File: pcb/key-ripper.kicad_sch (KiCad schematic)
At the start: 197 parts, among them J1 Conn_01x03, SW1 ESC, SW10 F9, SW11 F10, SW12 F11, SW13 F12, SW14 TILDE, SW15 1, SW16 2, SW17 3, SW18 4, SW19 5, SW2 F1, SW20 6, SW21 7, SW22 8, SW23 9, SW24 0, SW25 -, SW26 =, SW27 BACKSPACE, SW28 TAB, SW29 Q, SW3 F2, SW30 W, SW31 E, SW32 R, SW33 T, SW34 Y, SW35 U, SW36 I, SW37 O, SW38 P, SW39 [, SW4 F3, SW40 ], SW41 \, SW42 CAPS, SW43 A, SW44 S, SW45 D, SW46 F, SW47 G, SW48 H, SW49 J, SW5 F4, SW50 K, SW51 L, SW52 ;, SW53 ', SW54 ENTER, SW55 L_SHIFT, SW56 Z, SW57 X, SW58 C, SW59 V, SW6 F5, SW60 B, SW61 N, SW62 M, SW63 ,, SW64 ., SW65 /, SW66 UP, SW67 FN, SW68 BL_CTRL, SW69 L_ALT, SW7 F6, SW70 L_CMD, SW71 SPACE, SW72 R_CMD, SW73 LEFT, SW74 DOWN, SW75 RIGHT, SW8 F7, SW9 F8, U1 RP2040, U2 TYPE-C-31-M-12, U3 XC6206PxxxMR, U4 W25Q128JVS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

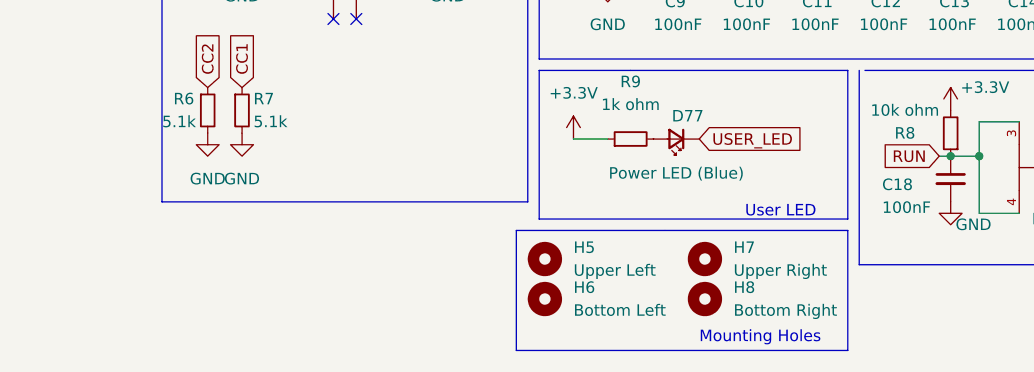
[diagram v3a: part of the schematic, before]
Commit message: Add M2 spacer pass-through mounting holes to the schematic
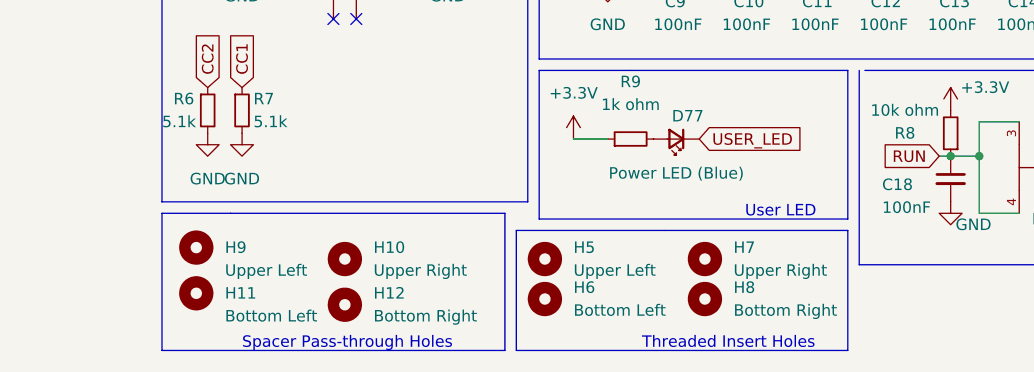
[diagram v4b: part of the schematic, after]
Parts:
- added H10: Upper Right, footprints:m2_hex_spacer_passthrough, symbol Mechanical:MountingHole
- added H11: Bottom Left, footprints:m2_hex_spacer_passthrough, symbol Mechanical:MountingHole
- added H12: Bottom Right, footprints:m2_hex_spacer_passthrough, symbol Mechanical:MountingHole
- added H9: Upper Left, footprints:m2_hex_spacer_passthrough, symbol Mechanical:MountingHole
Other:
- note added: "Spacer Pass-through Holes"
- note added: "Threaded Insert Holes"
- note removed: "Mounting Holes"
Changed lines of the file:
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@@
     (stroke (width 0) (type default) (color 0 0 0 0))
   )
+  (polyline (pts (xy 50.8 195.58) (xy 12.7 195.58))
+    (stroke (width 0) (type default) (color 0 0 0 0))
+  )
   (wire (pts (xy 22.86 92.71) (xy 26.67 92.71))
     (stroke (width 0) (type default) (color 0 0 0 0))
@@
     (stroke (width 0) (type default) (color 0 0 0 0))
   )
+  (polyline (pts (xy 50.8 180.34) (xy 50.8 195.58))
+    (stroke (width 0) (type default) (color 0 0 0 0))
+  )
   (wire (pts (xy 143.51 36.83) (xy 143.51 49.53))
     (stroke (width 0) (type default) (color 0 0 0 0))
@@
     (stroke (width 0) (type default) (color 0 0 0 0))
   )
+  (polyline (pts (xy 20.32 180.34) (xy 50.8 180.34))
+    (stroke (width 0) (type default) (color 0 0 0 0))
+  )
   (wire (pts (xy 113.03 62.23) (xy 113.03 74.93))
     (stroke (width 0) (type default) (color 0 0 0 0))
@@
     (stroke (width 0) (type default) (color 0 0 0 0))
   )
+  (polyline (pts (xy 12.7 180.34) (xy 20.32 180.34))
+    (stroke (width 0) (type default) (color 0 0 0 0))
+  )
   (wire (pts (xy -1.905 55.88) (xy 0.635 55.88))
     (stroke (width 0) (type default) (color 0 0 0 0))
@@
     (stroke (width 0) (type default) (color 0 0 0 0))
   )
+  (polyline (pts (xy 12.7 195.58) (xy 12.7 180.34))
+    (stroke (width 0) (type default) (color 0 0 0 0))
+  )
   (wire (pts (xy 231.775 123.19) (xy 231.775 118.745))
     (stroke (width 0) (type default) (color 0 0 0 0))
@@
     (effects (font (size 1.27 1.27)) (justify left bottom))
   )
-  (text "Mounting Holes" (at 72.39 194.945 0)
+  (text "Threaded Insert Holes" (at 66.04 195.58 0)
     (effects (font (size 1.27 1.27)) (justify left bottom))
   )
@@
     (effects (font (size 1.27 1.27)) (justify left bottom))
   )
+  (text "Spacer Pass-through Holes" (at 21.59 195.58 0)
+    (effects (font (size 1.27 1.27)) (justify left bottom))
+  )
   (text "Serial Wire Debug" (at 171.45 139.065 0)
     (effects (font (size 1.27 1.27)) (justify left bottom))
@@
     (pin "2")
   )
+  (symbol (lib_id "Mechanical:MountingHole") (at 33.02 185.42 0) (unit 1)
+    (in_bom yes) (on_board yes) (fields_autoplaced)
+    (property "Reference" "H10" (id 0) (at 36.195 184.1499 0)
+      (effects (font (size 1.27 1.27)) (justify left))
+    )
+    (property "Value" "Upper Right" (id 1) (at 36.195 186.6899 0)
+      (effects (font (size 1.27 1.27)) (justify left))
+    )
+    (property "Footprint" "footprints:m2_hex_spacer_passthrough" (id 2) (at 33.02 185.42 0)
+      (effects (font (size 1.27 1.27)) hide)
+    )
+    (property "Datasheet" "~" (id 3) (at 33.02 185.42 0)
+      (effects (font (size 1.27 1.27)) hide)
+    )
+  )
   (symbol (lib_id "Device:C_Small") (at 120.015 125.73 0) (unit 1)
     (in_bom yes) (on_board yes) (fields_autoplaced)
@@
     (pin "1")
   )
+  (symbol (lib_id "Mechanical:MountingHole") (at 33.02 190.5 0) (unit 1)
+    (in_bom yes) (on_board yes) (fields_autoplaced)
+    (property "Reference" "H12" (id 0) (at 36.195 189.2299 0)
+      (effects (font (size 1.27 1.27)) (justify left))
+    )
+    (property "Value" "Bottom Right" (id 1) (at 36.195 191.7699 0)
+      (effects (font (size 1.27 1.27)) (justify left))
+    )
+    (property "Footprint" "footprints:m2_hex_spacer_passthrough" (id 2) (at 33.02 190.5 0)
+      (effects (font (size 1.27 1.27)) hide)
+    )
+    (property "Datasheet" "~" (id 3) (at 33.02 190.5 0)
+      (effects (font (size 1.27 1.27)) hide)
+    )
+  )
   (symbol (lib_id "Device:D_Small") (at 72.39 77.47 90) (unit 1)
     (in_bom yes) (on_board yes)
@@
     (pin "2")
   )
+  (symbol (lib_id "Mechanical:MountingHole") (at 16.51 184.15 0) (unit 1)
+    (in_bom yes) (on_board yes)
+    (property "Reference" "H9" (id 0) (at 19.685 184.1499 0)
+      (effects (font (size 1.27 1.27)) (justify left))
+    )
+    (property "Value" "Upper Left" (id 1) (at 19.685 186.6899 0)
+      (effects (font (size 1.27 1.27)) (justify left))
+    )
+    (property "Footprint" "footprints:m2_hex_spacer_passthrough" (id 2) (at 16.51 184.15 0)
+      (effects (font (size 1.27 1.27)) hide)
+    )
+    (property "Datasheet" "~" (id 3) (at 16.51 184.15 0)
+      (effects (font (size 1.27 1.27)) hide)
+    )
+  )
   (symbol (lib_id "Device:C_Small") (at 107.95 151.765 0) (unit 1)
     (in_bom yes) (on_board yes)
@@
     (pin "2")
   )
+  (symbol (lib_id "Mechanical:MountingHole") (at 16.51 189.23 0) (unit 1)
+    (in_bom yes) (on_board yes)
+    (property "Reference" "H11" (id 0) (at 19.685 189.2299 0)
+      (effects (font (size 1.27 1.27)) (justify left))
+    )
+    (property "Value" "Bottom Left" (id 1) (at 19.685 191.7699 0)
+      (effects (font (size 1.27 1.27)) (justify left))
+    )
+    (property "Footprint" "footprints:m2_hex_spacer_passthrough" (id 2) (at 16.51 189.23 0)
+      (effects (font (size 1.27 1.27)) hide)
+    )
+    (property "Datasheet" "~" (id 3) (at 16.51 189.23 0)
+      (effects (font (size 1.27 1.27)) hide)
+    )
+  )
   (symbol (lib_id "Switch:SW_Push") (at 62.23 49.53 0) (unit 1)
     (in_bom yes) (on_board yes) (fields_autoplaced)
@@
       (reference "H8") (unit 1) (value "Bottom Right") (footprint "footprints:threaded_insert_m3_24939")
     )
+    (path "/b908f0d6-f276-4b53-8757-77900b0c31c4"
+      (reference "H9") (unit 1) (value "Upper Left") (footprint "footprints:m2_hex_spacer_passthrough")
+    )
+    (path "/751c73b9-913c-424a-a0fb-30ecc4a69248"
+      (reference "H10") (unit 1) (value "Upper Right") (footprint "footprints:m2_hex_spacer_passthrough")
+    )
+    (path "/c2a76fc2-6b67-49a3-ada5-bc5364302220"
+      (reference "H11") (unit 1) (value "Bottom Left") (footprint "footprints:m2_hex_spacer_passthrough")
+    )
+    (path "/7e1e60e5-bf93-4fda-b4a7-96c7ffe3f045"
+      (reference "H12") (unit 1) (value "Bottom Right") (footprint "footprints:m2_hex_spacer_passthrough")
+    )
     (path "/1b5afd94-2096-4603-93d6-8693d1fb5da2"

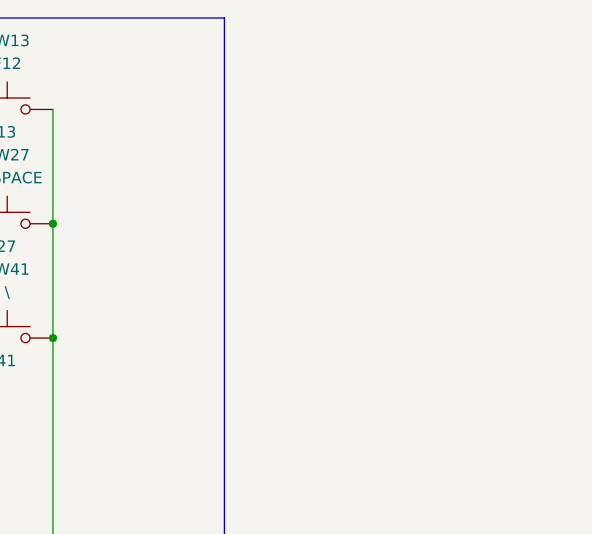
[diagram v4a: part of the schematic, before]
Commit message: Add footprints for the hex spacer pass-through edge cuts
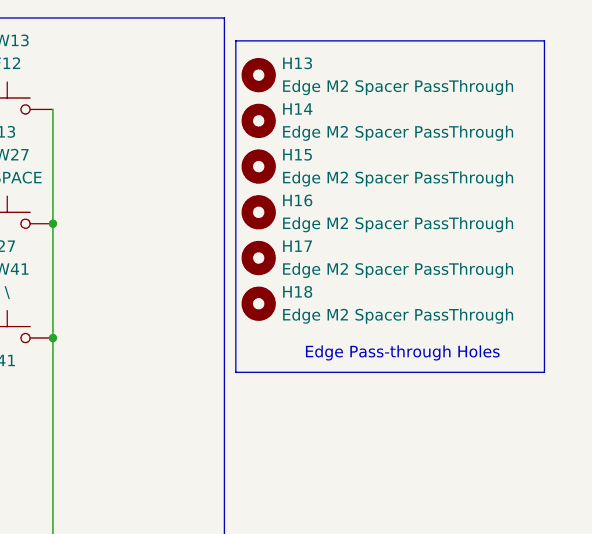
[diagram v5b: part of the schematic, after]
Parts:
- added H13, H14, H15, H16, H17, H18: Edge M2 Spacer PassThrough, footprints:m2_hex_spacer_passthrough_edge, symbol Mechanical:MountingHole
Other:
- note added: "Edge Pass-through Holes"
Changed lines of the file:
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@@
     (stroke (width 0) (type default) (color 0 0 0 0))
   )
+  (polyline (pts (xy 255.27 16.51) (xy 289.56 16.51))
+    (stroke (width 0) (type default) (color 0 0 0 0))
+  )
   (polyline (pts (xy 50.8 180.34) (xy 50.8 195.58))
     (stroke (width 0) (type default) (color 0 0 0 0))
@@
     (stroke (width 0) (type default) (color 0 0 0 0))
   )
+  (polyline (pts (xy 255.27 16.51) (xy 255.27 53.34))
+    (stroke (width 0) (type default) (color 0 0 0 0))
+  )
   (wire (pts (xy 77.47 154.305) (xy 85.09 154.305))
     (stroke (width 0) (type default) (color 0 0 0 0))
@@
     (stroke (width 0) (type default) (color 0 0 0 0))
   )
+  (polyline (pts (xy 289.56 16.51) (xy 289.56 53.34))
+    (stroke (width 0) (type default) (color 0 0 0 0))
+  )
   (wire (pts (xy 102.87 41.91) (xy 118.11 41.91))
     (stroke (width 0) (type default) (color 0 0 0 0))
@@
     (stroke (width 0) (type default) (color 0 0 0 0))
   )
+  (polyline (pts (xy 289.56 53.34) (xy 255.27 53.34))
+    (stroke (width 0) (type default) (color 0 0 0 0))
+  )
   (wire (pts (xy -38.1 43.18) (xy -41.91 43.18))
     (stroke (width 0) (type default) (color 0 0 0 0))
@@
     (effects (font (size 1.27 1.27)) (justify left bottom))
   )
+  (text "Edge Pass-through Holes" (at 262.89 52.07 0)
+    (effects (font (size 1.27 1.27)) (justify left bottom))
+  )
   (text "Stabilizers" (at 147.32 187.325 0)
     (effects (font (size 1.27 1.27)) (justify left bottom))
@@
     (pin "B9")
   )
+  (symbol (lib_id "Mechanical:MountingHole") (at 257.81 20.32 0) (unit 1)
+    (in_bom yes) (on_board yes) (fields_autoplaced)
+    (property "Reference" "H13" (id 0) (at 260.35 19.0499 0)
+      (effects (font (size 1.27 1.27)) (justify left))
+    )
+    (property "Value" "Edge M2 Spacer PassThrough" (id 1) (at 260.35 21.5899 0)
+      (effects (font (size 1.27 1.27)) (justify left))
+    )
+    (property "Footprint" "footprints:m2_hex_spacer_passthrough_edge" (id 2) (at 257.81 20.32 0)
+      (effects (font (size 1.27 1.27)) hide)
+    )
+    (property "Datasheet" "~" (id 3) (at 257.81 20.32 0)
+      (effects (font (size 1.27 1.27)) hide)
+    )
+  )
   (symbol (lib_id "Device:D_Small") (at 133.35 26.67 90) (unit 1)
     (in_bom yes) (on_board yes)
@@
     (pin "1")
   )
+  (symbol (lib_id "Mechanical:MountingHole") (at 257.81 30.48 0) (unit 1)
+    (in_bom yes) (on_board yes) (fields_autoplaced)
+    (property "Reference" "H15" (id 0) (at 260.35 29.2099 0)
+      (effects (font (size 1.27 1.27)) (justify left))
+    )
+    (property "Value" "Edge M2 Spacer PassThrough" (id 1) (at 260.35 31.7499 0)
+      (effects (font (size 1.27 1.27)) (justify left))
+    )
+    (property "Footprint" "footprints:m2_hex_spacer_passthrough_edge" (id 2) (at 257.81 30.48 0)
+      (effects (font (size 1.27 1.27)) hide)
+    )
+    (property "Datasheet" "~" (id 3) (at 257.81 30.48 0)
+      (effects (font (size 1.27 1.27)) hide)
+    )
+  )
   (symbol (lib_id "Device:D_Small") (at 224.79 26.67 90) (unit 1)
     (in_bom yes) (on_board yes)
@@
     )
   )
+  (symbol (lib_id "Mechanical:MountingHole") (at 257.81 35.56 0) (unit 1)
+    (in_bom yes) (on_board yes) (fields_autoplaced)
+    (property "Reference" "H16" (id 0) (at 260.35 34.2899 0)
+      (effects (font (size 1.27 1.27)) (justify left))
+    )
+    (property "Value" "Edge M2 Spacer PassThrough" (id 1) (at 260.35 36.8299 0)
+      (effects (font (size 1.27 1.27)) (justify left))
+    )
+    (property "Footprint" "footprints:m2_hex_spacer_passthrough_edge" (id 2) (at 257.81 35.56 0)
+      (effects (font (size 1.27 1.27)) hide)
+    )
+    (property "Datasheet" "~" (id 3) (at 257.81 35.56 0)
+      (effects (font (size 1.27 1.27)) hide)
+    )
+  )
   (symbol (lib_id "power:+3.3V") (at -90.17 35.56 0) (unit 1)
     (in_bom yes) (on_board yes) (fields_autoplaced)
@@
     (pin "2")
   )
+  (symbol (lib_id "Mechanical:MountingHole") (at 257.81 45.72 0) (unit 1)
+    (in_bom yes) (on_board yes) (fields_autoplaced)
+    (property "Reference" "H18" (id 0) (at 260.35 44.4499 0)
+      (effects (font (size 1.27 1.27)) (justify left))
+    )
+    (property "Value" "Edge M2 Spacer PassThrough" (id 1) (at 260.35 46.9899 0)
+      (effects (font (size 1.27 1.27)) (justify left))
+    )
+    (property "Footprint" "footprints:m2_hex_spacer_passthrough_edge" (id 2) (at 257.81 45.72 0)
+      (effects (font (size 1.27 1.27)) hide)
+    )
+    (property "Datasheet" "~" (id 3) (at 257.81 45.72 0)
+      (effects (font (size 1.27 1.27)) hide)
+    )
+  )
   (symbol (lib_id "Device:D_Small") (at 72.39 64.77 90) (unit 1)
     (in_bom yes) (on_board yes)
@@
     (pin "2")
   )
+  (symbol (lib_id "Mechanical:MountingHole") (at 257.81 40.64 0) (unit 1)
+    (in_bom yes) (on_board yes) (fields_autoplaced)
+    (property "Reference" "H17" (id 0) (at 260.35 39.3699 0)
+      (effects (font (size 1.27 1.27)) (justify left))
+    )
+    (property "Value" "Edge M2 Spacer PassThrough" (id 1) (at 260.35 41.9099 0)
+      (effects (font (size 1.27 1.27)) (justify left))
+    )
+    (property "Footprint" "footprints:m2_hex_spacer_passthrough_edge" (id 2) (at 257.81 40.64 0)
+      (effects (font (size 1.27 1.27)) hide)
+    )
+    (property "Datasheet" "~" (id 3) (at 257.81 40.64 0)
+      (effects (font (size 1.27 1.27)) hide)
+    )
+  )
   (symbol (lib_id "Device:D_Small") (at 194.31 90.17 90) (unit 1)
     (in_bom yes) (on_board yes)
@@
     (pin "2")
   )
+  (symbol (lib_id "Mechanical:MountingHole") (at 257.81 25.4 0) (unit 1)
+    (in_bom yes) (on_board yes) (fields_autoplaced)
+    (property "Reference" "H14" (id 0) (at 260.35 24.1299 0)
+      (effects (font (size 1.27 1.27)) (justify left))
+    )
+    (property "Value" "Edge M2 Spacer PassThrough" (id 1) (at 260.35 26.6699 0)
+      (effects (font (size 1.27 1.27)) (justify left))
+    )
+    (property "Footprint" "footprints:m2_hex_spacer_passthrough_edge" (id 2) (at 257.81 25.4 0)
+      (effects (font (size 1.27 1.27)) hide)
+    )
+    (property "Datasheet" "~" (id 3) (at 257.81 25.4 0)
+      (effects (font (size 1.27 1.27)) hide)
+    )
+  )
   (symbol (lib_id "Device:D_Small") (at 41.91 52.07 90) (unit 1)
     (in_bom yes) (on_board yes)
@@
       (reference "H12") (unit 1) (value "Bottom Right") (footprint "footprints:m2_hex_spacer_passthrough")
     )
+    (path "/398dbff6-894b-4a1a-9bd6-b9b822a75720"
+      (reference "H13") (unit 1) (value "Edge M2 Spacer PassThrough") (footprint "footprints:m2_hex_spacer_passthrough_edge")
+    )
+    (path "/dc18ad55-bbfa-4352-b739-f694bca71168"
+      (reference "H14") (unit 1) (value "Edge M2 Spacer PassThrough") (footprint "footprints:m2_hex_spacer_passthrough_edge")
+    )
+    (path "/80c5ac54-f77f-4752-84fb-c29d55e77da1"
+      (reference "H15") (unit 1) (value "Edge M2 Spacer PassThrough") (footprint "footprints:m2_hex_spacer_passthrough_edge")
+    )
+    (path "/907cc925-050f-4a60-b4eb-d1411497d26d"
+      (reference "H16") (unit 1) (value "Edge M2 Spacer PassThrough") (footprint "footprints:m2_hex_spacer_passthrough_edge")
+    )
+    (path "/bfedfdf6-4e0b-4688-9cee-fc4a8f2cba22"
+      (reference "H17") (unit 1) (value "Edge M2 Spacer PassThrough") (footprint "footprints:m2_hex_spacer_passthrough_edge")
+    )
+    (path "/b263b699-4ffc-4e92-ab87-99a2b979c54b"
+      (reference "H18") (unit 1) (value "Edge M2 Spacer PassThrough") (footprint "footprints:m2_hex_spacer_passthrough_edge")
+    )
     (path "/1b5afd94-2096-4603-93d6-8693d1fb5da2"

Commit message: Add various test points
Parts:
- added TP1: OSC_OUT, TestPoint:TestPoint_Pad_D1.0mm, symbol Connector:TestPoint_Small
- added TP10: QSPI_SS, TestPoint:TestPoint_Pad_D1.0mm, symbol Connector:TestPoint_Small
- added TP11: RUN, TestPoint:TestPoint_Pad_D1.0mm, symbol Connector:TestPoint_Small
- added TP12: 3v3, TestPoint:TestPoint_Pad_D1.0mm, symbol Connector:TestPoint_Small
- added TP2: +5V, TestPoint:TestPoint_Pad_D1.0mm, symbol Connector:TestPoint_Small
- added TP3: OSC_IN, TestPoint:TestPoint_Pad_D1.0mm, symbol Connector:TestPoint_Small
- added TP4: GND, TestPoint:TestPoint_Pad_D1.0mm, symbol Connector:TestPoint_Small
- added TP5: QSPI_SD0, TestPoint:TestPoint_Pad_D1.0mm, symbol Connector:TestPoint_Small
- added TP6: QSPI_SD1, TestPoint:TestPoint_Pad_D1.0mm, symbol Connector:TestPoint_Small
- added TP7: QSPI_SD2, TestPoint:TestPoint_Pad_D1.0mm, symbol Connector:TestPoint_Small
- added TP8: QSPI_SD3, TestPoint:TestPoint_Pad_D1.0mm, symbol Connector:TestPoint_Small
- added TP9: QSPI_SCLK, TestPoint:TestPoint_Pad_D1.0mm, symbol Connector:TestPoint_Small
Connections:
- net +3V3: now also TP12.1
- net +5V: now also TP2.1
- net GND: now also TP4.1
- net OSC_IN: now also TP3.1
- net OSC_OUT: now also TP1.1
- net QSPI_SCLK: now also TP9.1
- net QSPI_SD0: now also TP5.1
- net QSPI_SD1: now also TP6.1
- net QSPI_SD2: now also TP7.1
- net QSPI_SD3: now also TP8.1
- net QSPI_SS: now also TP10.1
- net RUN: now also TP11.1
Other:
- moved on the sheet: H13, H14, H15, H16, H17, H18, R5, U5

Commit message: Move resistors to 1608 metric size
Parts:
- R3, R4, R5, R6, R7, R8, R9: footprint Resistor_SMD:R_0402_1005Metric -> Resistor_SMD:R_0603_1608Metric
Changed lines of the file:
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@@
     (property "Reference" "R4" (id 0) (at 203.835 121.285 90))
     (property "Value" "10k ohm" (id 1) (at 201.295 121.285 90))
-    (property "Footprint" "Resistor_SMD:R_0402_1005Metric" (id 2) (at 205.74 121.285 0)
+    (property "Footprint" "Resistor_SMD:R_0603_1608Metric" (id 2) (at 205.74 121.285 0)
       (effects (font (size 1.27 1.27)) hide)
     )
@@
     (property "Reference" "R5" (id 0) (at 166.37 153.035 90))
     (property "Value" "1k ohm" (id 1) (at 166.37 155.575 90))
-    (property "Footprint" "Resistor_SMD:R_0402_1005Metric" (id 2) (at 166.37 151.13 0)
+    (property "Footprint" "Resistor_SMD:R_0603_1608Metric" (id 2) (at 166.37 151.13 0)
       (effects (font (size 1.27 1.27)) hide)
     )
@@
     (property "Reference" "R9" (id 0) (at 64.77 165.735 90))
     (property "Value" "1k ohm" (id 1) (at 64.77 168.275 90))
-    (property "Footprint" "Resistor_SMD:R_0402_1005Metric" (id 2) (at 64.77 172.085 0)
+    (property "Footprint" "Resistor_SMD:R_0603_1608Metric" (id 2) (at 64.77 172.085 0)
       (effects (font (size 1.27 1.27)) hide)
     )
@@
       (effects (font (size 1.27 1.27)) (justify left))
     )
-    (property "Footprint" "Resistor_SMD:R_0402_1005Metric" (id 2) (at 17.78 168.91 0)
+    (property "Footprint" "Resistor_SMD:R_0603_1608Metric" (id 2) (at 17.78 168.91 0)
       (effects (font (size 1.27 1.27)) hide)
     )
@@
       (effects (font (size 1.27 1.27)) (justify left))
     )
-    (property "Footprint" "Resistor_SMD:R_0402_1005Metric" (id 2) (at 21.59 168.91 0)
+    (property "Footprint" "Resistor_SMD:R_0603_1608Metric" (id 2) (at 21.59 168.91 0)
       (effects (font (size 1.27 1.27)) hide)
     )
@@
     (property "Reference" "R8" (id 0) (at 95.25 171.45 0))
     (property "Value" "10k ohm" (id 1) (at 95.25 168.91 0))
-    (property "Footprint" "Resistor_SMD:R_0402_1005Metric" (id 2) (at 100.33 171.45 0)
+    (property "Footprint" "Resistor_SMD:R_0603_1608Metric" (id 2) (at 100.33 171.45 0)
       (effects (font (size 1.27 1.27)) hide)
     )
@@
     (property "Reference" "R3" (id 0) (at -99.695 106.045 90))
     (property "Value" "1k ohm" (id 1) (at -99.695 108.585 90))
-    (property "Footprint" "Resistor_SMD:R_0402_1005Metric" (id 2) (at -99.695 104.14 0)
+    (property "Footprint" "Resistor_SMD:R_0603_1608Metric" (id 2) (at -99.695 104.14 0)
       (effects (font (size 1.27 1.27)) hide)
     )
@@
     )
     (path "/e3a59236-f08b-40ae-bc75-a0d6e7e2a9e2"
-      (reference "R3") (unit 1) (value "1k ohm") (footprint "Resistor_SMD:R_0402_1005Metric")
+      (reference "R3") (unit 1) (value "1k ohm") (footprint "Resistor_SMD:R_0603_1608Metric")
     )
     (path "/0673e87d-59a0-44b4-ad99-f1df572f5ad5"
-      (reference "R4") (unit 1) (value "10k ohm") (footprint "Resistor_SMD:R_0402_1005Metric")
+      (reference "R4") (unit 1) (value "10k ohm") (footprint "Resistor_SMD:R_0603_1608Metric")
     )
     (path "/3db3f76d-bf7a-4abd-8b5f-28ad937f4bed"
-      (reference "R5") (unit 1) (value "1k ohm") (footprint "Resistor_SMD:R_0402_1005Metric")
+      (reference "R5") (unit 1) (value "1k ohm") (footprint "Resistor_SMD:R_0603_1608Metric")
     )
     (path "/8581ca9d-782d-4ccd-ae4b-6ba24e984a88"
-      (reference "R6") (unit 1) (value "5.1k") (footprint "Resistor_SMD:R_0402_1005Metric")
+      (reference "R6") (unit 1) (value "5.1k") (footprint "Resistor_SMD:R_0603_1608Metric")
     )
     (path "/b67c50d6-9af7-4802-a20c-e04cd7ad147b"
-      (reference "R7") (unit 1) (value "5.1k") (footprint "Resistor_SMD:R_0402_1005Metric")
+      (reference "R7") (unit 1) (value "5.1k") (footprint "Resistor_SMD:R_0603_1608Metric")
     )
     (path "/b73090dc-9a97-444f-98b7-722e87af29c5"
-      (reference "R8") (unit 1) (value "10k ohm") (footprint "Resistor_SMD:R_0402_1005Metric")
+      (reference "R8") (unit 1) (value "10k ohm") (footprint "Resistor_SMD:R_0603_1608Metric")
     )
     (path "/556ef9ca-0364-4889-be76-ec9d7d5619ff"
-      (reference "R9") (unit 1) (value "1k ohm") (footprint "Resistor_SMD:R_0402_1005Metric")
+      (reference "R9") (unit 1) (value "1k ohm") (footprint "Resistor_SMD:R_0603_1608Metric")
     )
     (path "/e7893166-2c2c-41b4-bd84-76ebc2e06551"
